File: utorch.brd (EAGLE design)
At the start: 20.6 x 12 mm, 24 parts, among them IC1 LTC4062, IC2 LTC3454, U1 2N7002BKW, X1 USB-MICROB

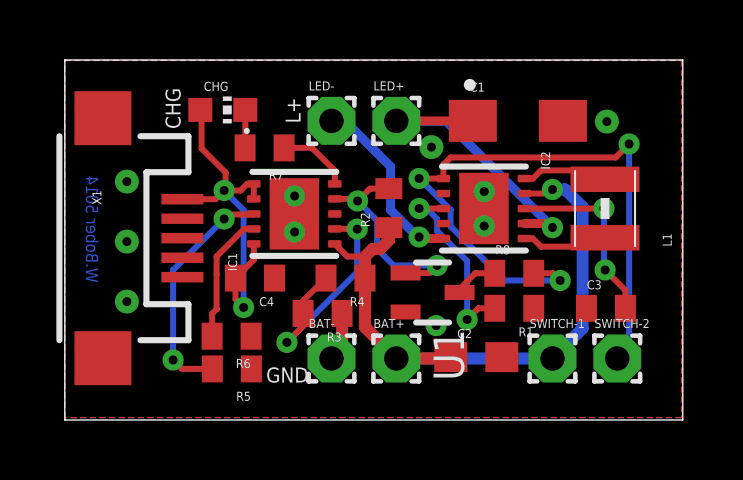
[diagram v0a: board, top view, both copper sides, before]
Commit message: Fixed on/off logic
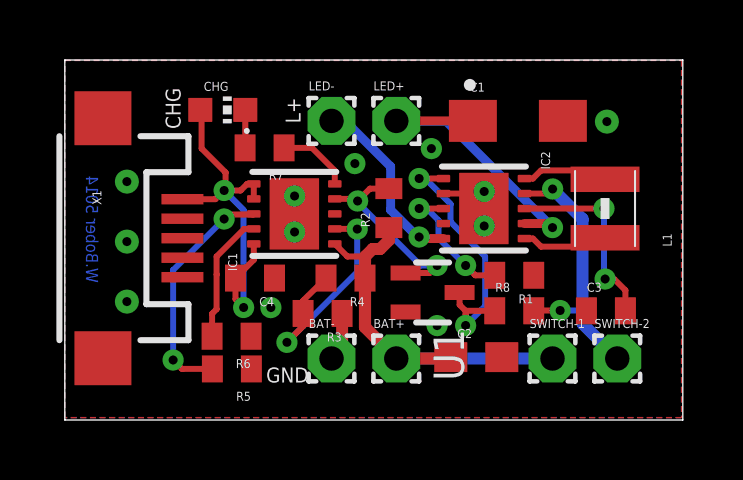
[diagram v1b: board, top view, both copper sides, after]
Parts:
- moved R8 1.25 mm to (23.9, 7.64)
- moved R1 1.10 mm to (23.9, 8.82)
- moved C3 0.08 mm to (26.9, 7.64)
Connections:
- removed net N$15: BAT+.1, C2.1, IC1.1, IC2.9, R2.1, R4.1, SWITCH-1.1
- new net BAT+: BAT+.1, C2.1, IC1.1, R2.1, R4.1, SWITCH-1.1
- net GND: now also IC2.2
- net N$16: now also IC2.1
- net N$7: now also IC2.9; no longer IC2.1
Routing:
- net N$15: track 21.2 -> 0.00 mm, vias 1 -> 0
- net BAT+: track 0.00 -> 13.5 mm
- net N$7: track 22.5 -> 9.63 mm, vias 3 -> 2
- net N$16: track 1.51 -> 9.61 mm, vias 0 -> 2
- net N$5: track 6.50 -> 4.71 mm
- net GND: track 1.65 -> 3.07 mm, vias 10 -> 12
- net N$10: track 7.53 -> 7.00 mm

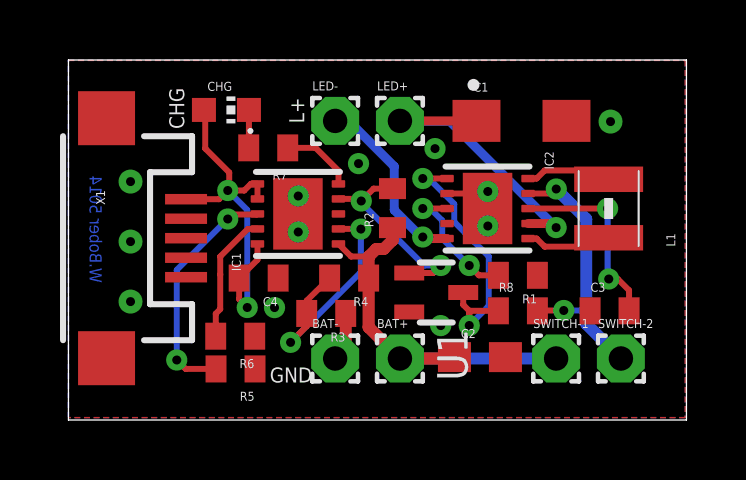
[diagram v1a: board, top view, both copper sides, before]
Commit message: Increased LED traces width to 0.35mm. Added FAB files.
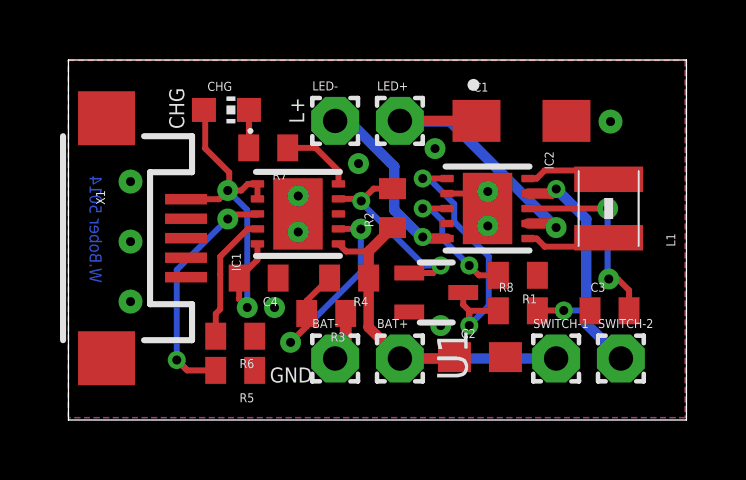
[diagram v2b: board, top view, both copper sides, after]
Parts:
- moved R5 0.05 mm to (14.4, 5.65)

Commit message: Fixed ltc4062 enable pin...
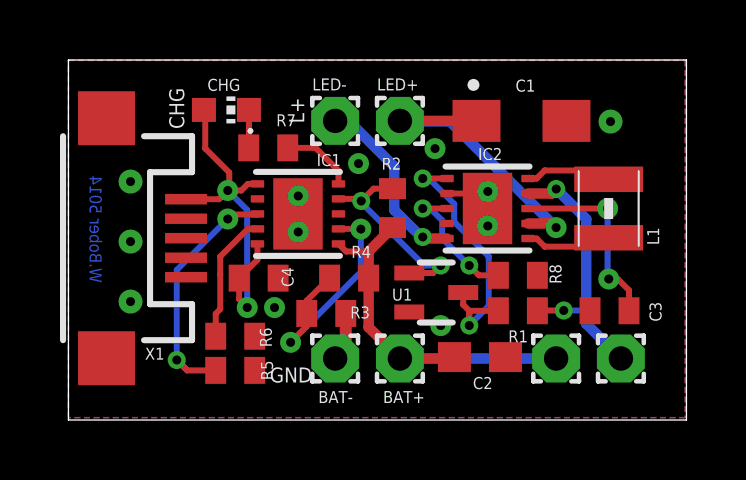
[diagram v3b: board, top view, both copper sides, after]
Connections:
- net N$14: no longer IC1.7
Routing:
- net N$14: track 12.9 -> 12.4 mm

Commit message: inital update
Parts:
- removed CHG: (no value), adl_lib_001:CHIP-LED0603
- removed R2: 100k 5%, adl_lib_001:ADL_LIB_001_R0402
- removed R7: 560 5%, resistor:R0402
- removed U1: 2N7002BKW, WB:SOT323
- added C5: 4.7uF, rcl:C0603
- added IC3: TINY13V-10MM0, atmel:10M1
- added IC4: TINY24/44/84-MU, avr-4:QFN/MLF20
- added LED1, LED2, LED3, LED4: (no value), led:CHIPLED_1206
- added R9: 0.05R 1%, adl_lib_001:ADL_LIB_001_R0402
- added U2: LTC4150, mike-temp:MSOP10
- moved R5 16.7 mm to (13.6, 22.3), turned to 0 degrees
- moved SWITCH-2 16.0 mm to (11.7, 9.26), turned to 90 degrees
- moved SWITCH-1 14.4 mm to (11.7, 11.2), turned to 90 degrees
- moved R6 13.1 mm to (15.2, 19.9), turned to 90 degrees
- moved R3 12.4 mm to (20.8, 19.5), turned to 90 degrees
- moved R4 10.8 mm to (19.7, 19.5), turned to 90 degrees
- moved C4 10.6 mm to (17.3, 19.1)
- moved IC1 10.4 mm to (17.5, 21.3)
- moved LED+ 8.77 mm to (23.5, 22.0)
- moved LED- 8.77 mm to (21.4, 22.0)
- moved C1 8.54 mm to (27.0, 22.0)
- moved C3 8.06 mm to (27.9, 15.6)
- moved IC2 8.06 mm to (23.9, 19.0)
- moved L1 8.06 mm to (27.9, 19.0)
- moved R8 8.06 mm to (24.9, 15.6)
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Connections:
- removed net N$12: IC1.5, R7.1
- removed net N$13: CHG.C, R7.2
- new net N$15: BAT+.1, R9.2, U2.1
- new net N$17: C5.2, U2.4
- new net N$18: C5.1, U2.3
- new net N$19: U2.10, U2.9
- new net N$22: U2.6
- new net VCC: IC3.10, IC4.9
- new net VDD: U2.8
- net BAT+: now also R9.1, U2.2; no longer BAT+.1, R2.1
- net GND: now also IC3.11, IC3.5, IC4.8, U2.7; no longer U1.2
- net N$10: no longer R2.2, U1.1
- net N$14: no longer CHG.A
- net N$16: no longer U1.3
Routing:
- net BAT+: track 13.3 -> 0.00 mm
- net N$14: track 12.4 -> 3.46 mm, vias 2 -> 1
- net N$4: track 10.2 -> 4.03 mm
- net N$10: track 7.00 -> 1.08 mm, vias 2 -> 1
- net N$11: track 8.18 -> 2.49 mm, vias 2 -> 0
- net N$8: track 8.33 -> 2.79 mm, vias 2 -> 0
- net N$3: track 6.20 -> 0.91 mm
- net N$9: track 4.34 -> 1.09 mm
- net N$12: track 2.48 -> 0.00 mm
- net GND: track 3.07 -> 1.43 mm, vias 12 -> 8
- net N$7: track 9.63 -> 7.99 mm
- net N$13: track 1.27 -> 0.00 mm
- net N$16: track 9.61 -> 8.75 mm
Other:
- board size 20.6 x 12 mm -> 20.6 x 17.2 mm

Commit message: something
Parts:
- removed IC4: TINY24/44/84-MU, avr-4:QFN/MLF20
- IC3: value TINY13V-10MM0 -> TINY24/44/84; device atmel:10M1 -> avr-7:QFN20-3X3
- moved IC3 26.3 mm to (15.2, 10.5)
- moved BAT- 4.20 mm to (18.6, 9.15), turned to 180 degrees
- moved LED1 4.00 mm to (23.6, 10.8), turned to 180 degrees
- moved LED4 3.58 mm to (28.9, 10.8), turned to 180 degrees
- moved C2 1.99 mm to (19.7, 11.4), turned to 180 degrees
- moved LED3 1.59 mm to (25.4, 10.8), turned to 180 degrees
- moved LED2 1.14 mm to (27.1, 10.8), turned to 180 degrees
- moved BAT+ 1.02 mm to (21.0, 9.15), turned to 180 degrees
- moved R9 0.10 mm to (20.8, 14.0)
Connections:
- removed net N$22: U2.6
- removed net VDD: U2.8
- new net INT: IC3.1, U2.10, U2.9
- new net LED-ENABLE: IC2.1, IC3.4, R8.1
- new net LOW-BAT: IC1.4, IC3.3
- new net N$21: IC3.13, LED1.C
- new net POL: IC3.2, U2.6
- net BAT+: now also IC2.9, R8.2; no longer SWITCH-1.1
- net GND: now also IC3.8, IC3.EXP, SWITCH-2.1; no longer IC3.11, IC3.5, IC4.8
- net N$10: now also IC3.11, LED4.C; no longer IC1.4
- net N$15: now also U2.8
- net N$16: now also IC3.12, LED3.C; no longer IC2.1, R8.1
- net N$19: now also IC3.14, LED2.C; no longer U2.10, U2.9
- net N$7: now also IC3.5, SWITCH-1.1; no longer IC2.9, R8.2, SWITCH-2.1
- net VCC: now also IC3.9; no longer IC3.10, IC4.9
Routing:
- net N$16: track 8.75 -> 0.00 mm, vias 2 -> 0
- net LED-ENABLE: track 0.00 -> 8.75 mm, vias 0 -> 2
- net N$7: track 7.99 -> 0.00 mm, vias 2 -> 0
- net BAT+: track 0.00 -> 7.98 mm, vias 0 -> 2
- net N$10: track 1.08 -> 0.00 mm, vias 1 -> 0
- net LOW-BAT: track 0.00 -> 1.08 mm, vias 0 -> 1
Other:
- board size 20.6 x 17.2 mm -> 20.6 x 16.2 mm
